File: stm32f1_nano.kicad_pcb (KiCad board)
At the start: 2 copper layers, 43.2 x 17.8 mm, 45 parts, among them J1 Analog, J2 Digital, J3 TYPE-C-31-M-12, J5 DEBUG, U1 STM32F103C8T6, U2 W25Q128JVSIQ, U4 XC6206P332MR, U5 AMS1117-5.0, Y1 X322516MLB4SI

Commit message: Change version
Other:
- board text added: "easy-smart.ch STM32F1 Nano ${REVISION}"
- board text removed: "easy-smart.ch STM32F1 Nano v1.0.1"
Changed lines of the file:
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@@
   (paper "A4")
   (title_block
-    (date "sam. 04 avril 2015")
+    (title "STM32F1 Nano")
+    (date "2023-09-05")
+    (rev "1.1.x-dev")
+    (company "easy-smart solution GmbH")
   )
   (layers
@@
     (effects (font (size 1 1) (thickness 0.15)) (justify left mirror))
   )
-  (gr_text "easy-smart.ch\nSTM32F1 Nano\nv1.0.1" (at 100.762 91.11 90) (layer "B.SilkS")
+  (gr_text "easy-smart.ch\nSTM32F1 Nano\n${REVISION}" (at 100.762 91.11 90) (layer "B.SilkS")
     (effects (font (size 0.8 0.6) (thickness 0.08)) (justify top mirror))
   )

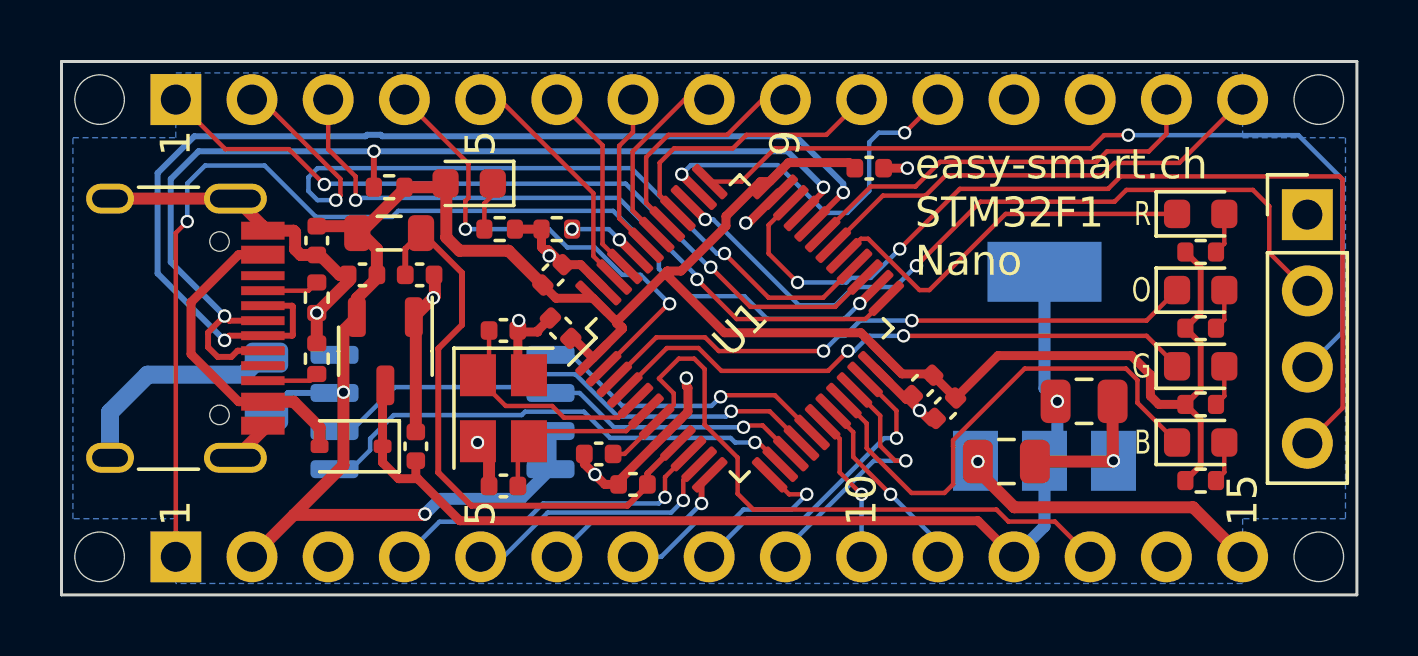
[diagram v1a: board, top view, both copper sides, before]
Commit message: #1 Make debug pins compatible with BluePill
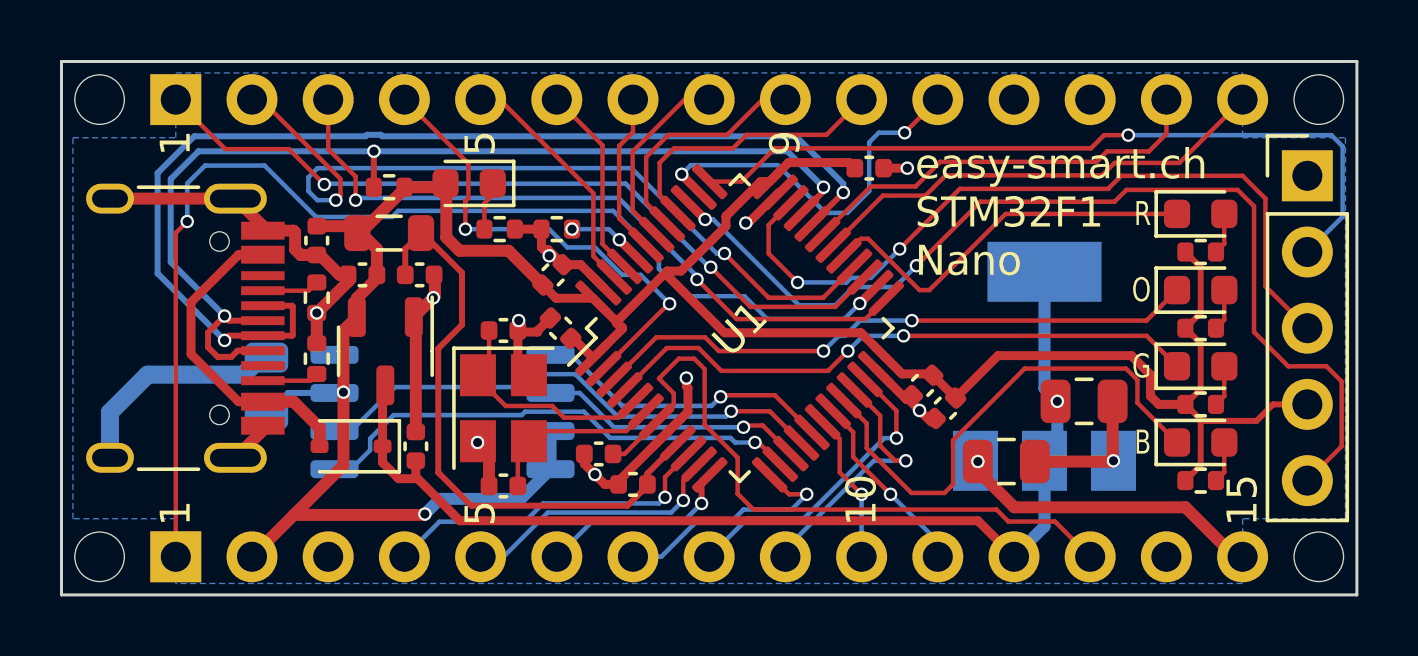
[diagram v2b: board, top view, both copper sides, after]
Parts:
- C12: value 100n 100V -> 100nF
- J5: footprint Connector_PinHeader_2.54mm:PinHeader_1x04_P2.54mm_Vertical -> Connector_PinHeader_2.54mm:PinHeader_1x05_P2.54mm_Vertical
- moved J5 1.30 mm to (141.5, 86.0)
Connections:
- J5 pad 2: SWO -> SWCLK
- J5 pad 3: SWCLK -> SWDIO
- J5 pad 4: SWDIO -> +3.3V
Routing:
- net SWO: track 25.2 -> 32.9 mm
- net SWDIO: track 32.3 -> 25.6 mm
- net +3.3V: track 82.5 -> 86.3 mm
- net SWCLK: track 29.1 -> 25.9 mm

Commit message: #5 Check PWM pins
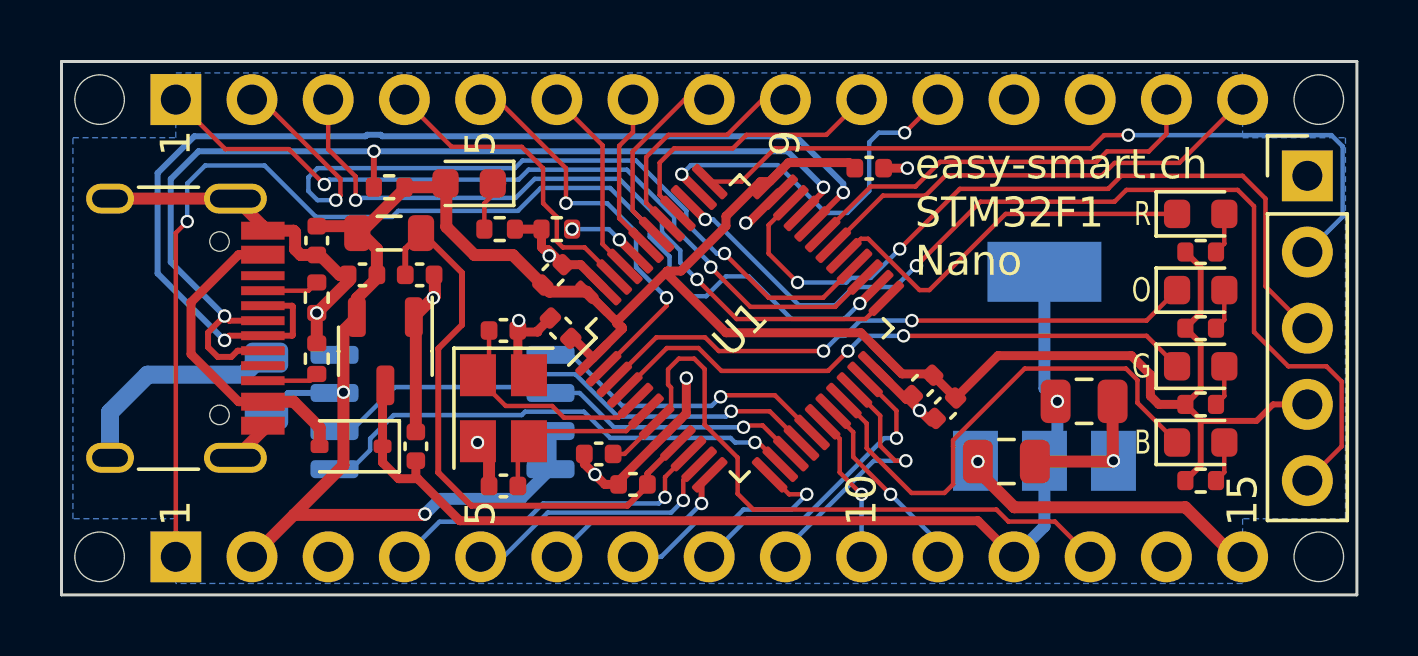
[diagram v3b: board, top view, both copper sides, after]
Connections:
- J2 pad 4: /PC13 -> /PB9
- J2 pad 5: /PB9 -> /PC13
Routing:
- net /PB9: track 7.50 -> 10.6 mm
- net /PC13: track 16.2 -> 13.5 mm
- net /PB13: track 38.0 -> 39.5 mm
- net /PB12: track 23.5 -> 24.4 mm
- net /PB14: track 26.3 -> 26.9 mm

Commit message: #4 Can U5 be moved to Front?
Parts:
- U5: moved to F.Cu
- moved C1 15.1 mm to (115.0, 89.3), turned to 45 degrees
- moved C16 4.07 mm to (130.6, 95.6), turned to 180 degrees
- moved C15 2.53 mm to (134.0, 95.6), turned to 180 degrees
- moved U5 2.29 mm to (132.3, 90.1)
- moved C2 1.34 mm to (128.2, 94.3), turned to -90 degrees
- moved C6 0.05 mm to (119.0, 96.3)
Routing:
- net /~{RESET}: track 22.6 -> 32.3 mm
- net +3.3V: track 86.0 -> 88.8 mm
- net +5V: track 35.7 -> 38.3 mm, vias 1 -> 2
- net /LED4_BLU: track 16.9 -> 19.2 mm
- net +12V: track 10.3 -> 8.16 mm, vias 1 -> 0
- net GND: track 49.7 -> 48.3 mm, vias 11 -> 12
- net SWDIO: track 25.6 -> 26.6 mm
- net SWO: track 32.9 -> 33.7 mm
- net /PB1: track 5.75 -> 6.47 mm
- net /PB11: track 10.3 -> 10.8 mm
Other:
- board text removed: "1"
- board text removed: "15"
- board text removed: "B"
- board text removed: "G"
- board text removed: "O"
- board text removed: "R"

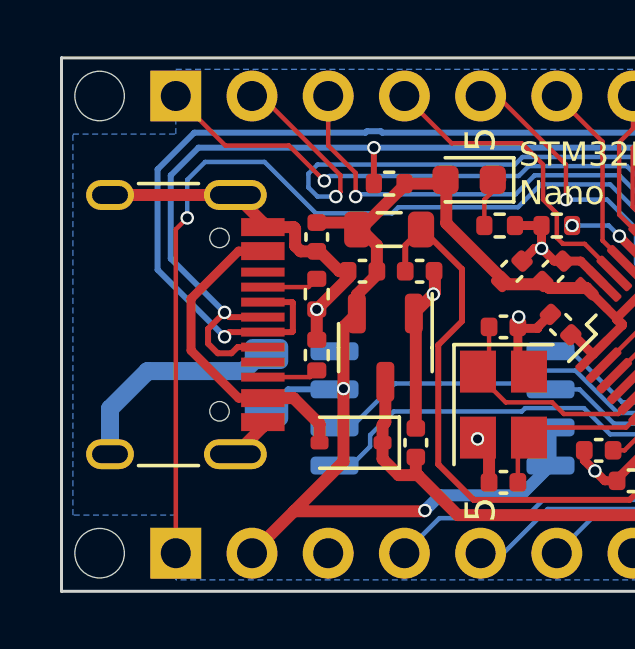
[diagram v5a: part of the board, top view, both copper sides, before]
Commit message: #10 Change USB connector to SHOU HAN TYPE-C 16PIN 2MD(073) (C2765186)
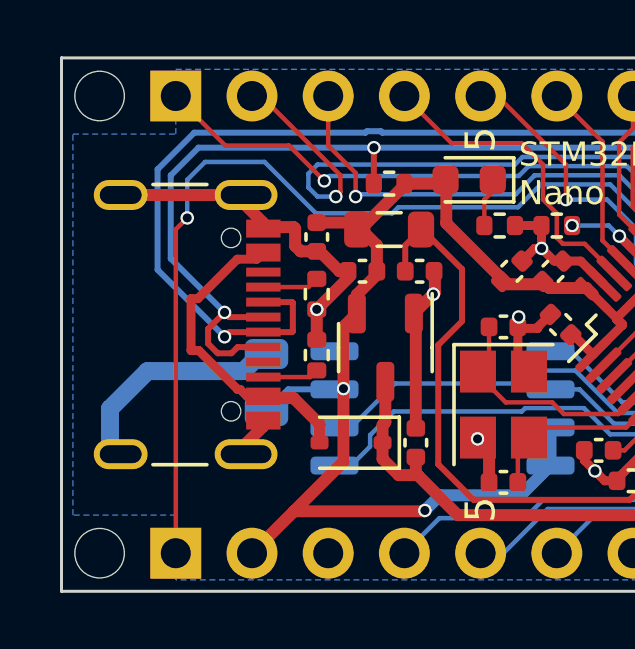
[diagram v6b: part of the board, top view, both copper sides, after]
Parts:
- C12: value 100nF -> 100n 100V
- J3: footprint Connector_USB:USB_C_Receptacle_HRO_TYPE-C-31-M-12 -> #Connector:SHOU HAN TYPE-C 16PIN 2MD(073)
- moved J3 0.38 mm to (103.0, 91.1)

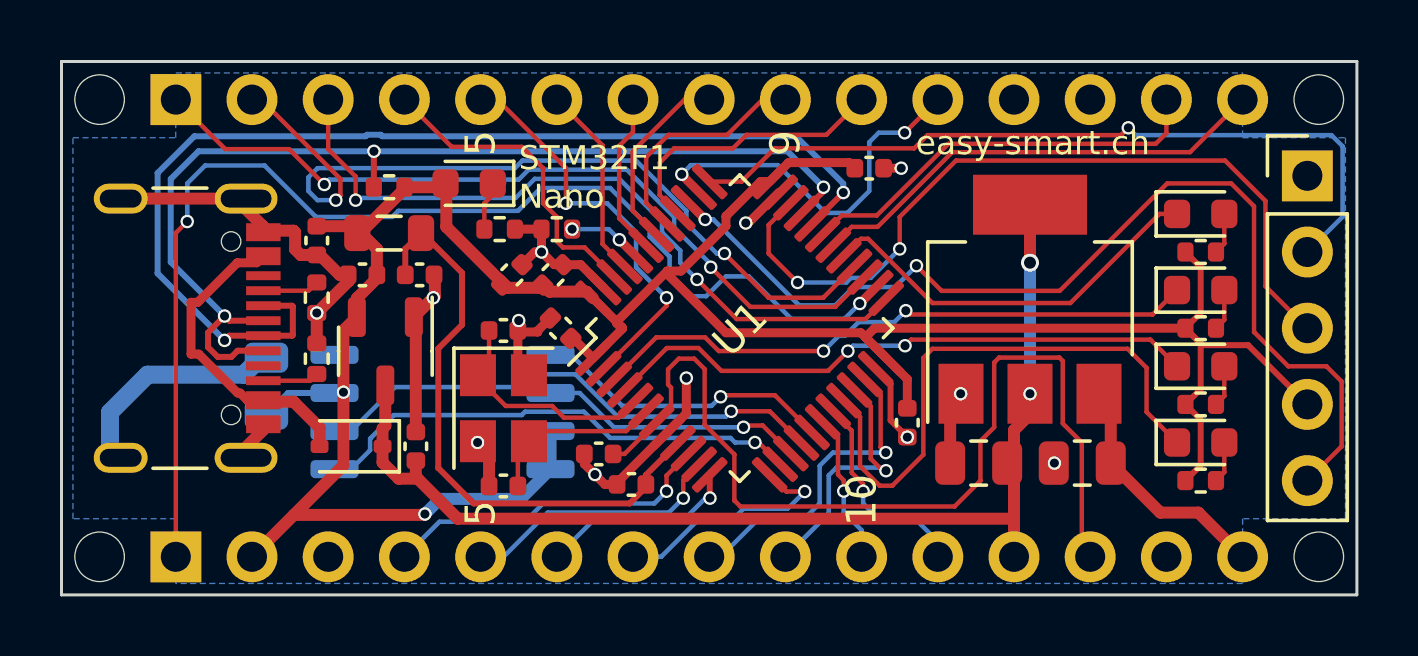
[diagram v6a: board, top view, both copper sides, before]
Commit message: #8 Use green power led
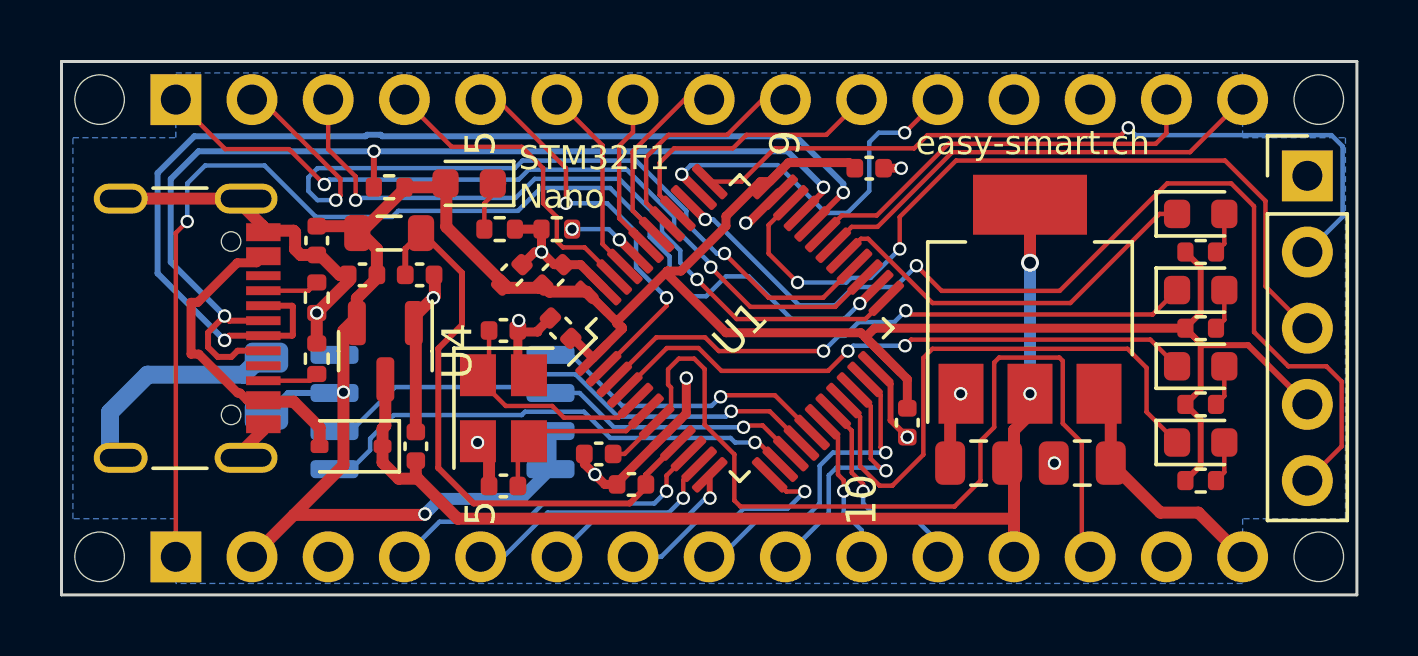
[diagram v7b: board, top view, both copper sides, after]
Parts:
- D8: value LED red (PWR) -> PWR LED (grn)
- R1: value 330 -> 200
- U4: footprint Package_TO_SOT_SMD:SOT-23-3 -> Package_TO_SOT_SMD:SOT-23
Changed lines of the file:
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@@
     (descr "Resistor SMD 0402 (1005 Metric), square (rectangular) end terminal, IPC_7351 nominal, (Body size source: IPC-SM-782 page 72, https://www.pcb-3d.com/wordpress/wp-content/uploads/ipc-sm-782a_amendment_1_and_2.pdf), generated with kicad-footprint-generator")
     (tags "resistor")
-    (property "Description" "62.5mW Thick Film Resistors ±100ppm/℃ ±1% 330Ω 0402  Chip Resistor - Surface Mount ROHS")
-    (property "JLCPCB Part #" "C25104")
+    (property "Description" "62.5mW Thick Film Resistors ±100ppm/℃ ±1% 200Ω 0402  Chip Resistor - Surface Mount ROHS")
+    (property "JLCPCB Part #" "C25087")
     (property "Manufacturer" "UNI-ROYAL(Uniroyal Elec)")
-    (property "Partnumber" "0402WGF3300TCE")
+    (property "Partnumber" "0402WGF2000TCE")
     (property "Sheetfile" "stm32f1_nano.kicad_sch")
     (property "Sheetname" "")
@@
         (effects (font (size 1 1) (thickness 0.15)))
     )
-    (fp_text value "330" (at 0 1.17) (layer "F.Fab")
+    (fp_text value "200" (at 0 1.17) (layer "F.Fab")
         (effects (font (size 1 1) (thickness 0.15)))
     )
@@
     )
   )
-  (footprint "Package_TO_SOT_SMD:SOT-23-3" (layer "F.Cu")
+  (footprint "Package_TO_SOT_SMD:SOT-23" (layer "F.Cu")
     (at 110.795 91.8775 -90)
-    (descr "SOT, 3 Pin (https://www.jedec.org/sites/default/files/docs/Mo-178D.PDF inferred 3-pin variant), generated with kicad-footprint-generator ipc_gullwing_generator.py")
+    (descr "SOT, 3 Pin (https://www.jedec.org/system/files/docs/to-236h.pdf variant AB), generated with kicad-footprint-generator ipc_gullwing_generator.py")
     (tags "SOT TO_SOT_SMD")
     (property "Description" "200mA Fixed 3.3V~3.3V Positive 6V SOT-23-3L  Linear Voltage Regulators (LDO) ROHS")
@@
     (property "ki_keywords" "Torex LDO Voltage Regulator Fixed Positive")
     (attr smd)
-    (fp_text reference "U4" (at 0 -2.4 90) (layer "F.SilkS") hide
-        (effects (font (size 1 1) (thickness 0.15)))
-    )
-    (fp_text value "XC6206P332MR" (at 0 2.4 90) (layer "F.Fab")
-        (effects (font (size 1 1) (thickness 0.15)))
-    )
-    (fp_text user "${REFERENCE}" (at 0 0 90) (layer "F.Fab")
-        (effects (font (size 0.4 0.4) (thickness 0.06)))
-    )
-    (fp_line (start 0 -1.56) (end -1.8 -1.56)
-      (stroke (width 0.12) (type solid)) (layer "F.SilkS"))
-    (fp_line (start 0 -1.56) (end 0.8 -1.56)
-      (stroke (width 0.12) (type solid)) (layer "F.SilkS"))
-    (fp_line (start 0 1.56) (end -0.8 1.56)
-      (stroke (width 0.12) (type solid)) (layer "F.SilkS"))
-    (fp_line (start 0 1.56) (end 0.8 1.56)
-      (stroke (width 0.12) (type solid)) (layer "F.SilkS"))
-    (fp_line (start -2.05 -1.7) (end -2.05 1.7)
-      (stroke (width 0.05) (type solid)) (layer "F.CrtYd"))
-    (fp_line (start -2.05 1.7) (end 2.05 1.7)
-      (stroke (width 0.05) (type solid)) (layer "F.CrtYd"))
-    (fp_line (start 2.05 -1.7) (end -2.05 -1.7)
-      (stroke (width 0.05) (type solid)) (layer "F.CrtYd"))
-    (fp_line (start 2.05 1.7) (end 2.05 -1.7)
-      (stroke (width 0.05) (type solid)) (layer "F.CrtYd"))
-    (fp_line (start -0.8 -1.05) (end -0.4 -1.45)
-      (stroke (width 0.1) (type solid)) (layer "F.Fab"))
-    (fp_line (start -0.8 1.45) (end -0.8 -1.05)
-      (stroke (width 0.1) (type solid)) (layer "F.Fab"))
-    (fp_line (start -0.4 -1.45) (end 0.8 -1.45)
-      (stroke (width 0.1) (type solid)) (layer "F.Fab"))
-    (fp_line (start 0.8 -1.45) (end 0.8 1.45)
-      (stroke (width 0.1) (type solid)) (layer "F.Fab"))
-    (fp_line (start 0.8 1.45) (end -0.8 1.45)
-      (stroke (width 0.1) (type solid)) (layer "F.Fab"))
-    (pad "1" smd roundrect (at -1.1375 -0.95 270) (size 1.325 0.6) (layers "F.Cu" "F.Paste" "F.Mask") (roundrect_rratio 0.25)
+    (fp_text reference "U4" (at 0 -2.4 -90) (layer "F.SilkS")
+        (effects (font (size 1 1) (thickness 0.15)))
+    )
+    (fp_text value "XC6206P332MR" (at 0 2.4 -90) (layer "F.Fab")
+        (effects (font (size 1 1) (thickness 0.15)))
+    )
+    (fp_text user "${REFERENCE}" (at 0 0 -90) (layer "F.Fab")
+        (effects (font (size 0.32 0.32) (thickness 0.05)))
+    )
+    (fp_line (start 0 -1.56) (end -1.675 -1.56)
+      (stroke (width 0.12) (type solid)) (layer "F.SilkS"))
+    (fp_line (start 0 -1.56) (end 0.65 -1.56)
+      (stroke (width 0.12) (type solid)) (layer "F.SilkS"))
+    (fp_line (start 0 1.56) (end -0.65 1.56)
+      (stroke (width 0.12) (type solid)) (layer "F.SilkS"))
+    (fp_line (start 0 1.56) (end 0.65 1.56)
+      (stroke (width 0.12) (type solid)) (layer "F.SilkS"))
+    (fp_line (start -1.92 -1.7) (end -1.92 1.7)
+      (stroke (width 0.05) (type solid)) (layer "F.CrtYd"))
+    (fp_line (start -1.92 1.7) (end 1.92 1.7)
+      (stroke (width 0.05) (type solid)) (layer "F.CrtYd"))
+    (fp_line (start 1.92 -1.7) (end -1.92 -1.7)
+      (stroke (width 0.05) (type solid)) (layer "F.CrtYd"))
+    (fp_line (start 1.92 1.7) (end 1.92 -1.7)
+      (stroke (width 0.05) (type solid)) (layer "F.CrtYd"))
+    (fp_line (start -0.65 -1.125) (end -0.325 -1.45)
+      (stroke (width 0.1) (type solid)) (layer "F.Fab"))
+    (fp_line (start -0.65 1.45) (end -0.65 -1.125)
+      (stroke (width 0.1) (type solid)) (layer "F.Fab"))
+    (fp_line (start -0.325 -1.45) (end 0.65 -1.45)
+      (stroke (width 0.1) (type solid)) (layer "F.Fab"))
+    (fp_line (start 0.65 -1.45) (end 0.65 1.45)
+      (stroke (width 0.1) (type solid)) (layer "F.Fab"))
+    (fp_line (start 0.65 1.45) (end -0.65 1.45)
+      (stroke (width 0.1) (type solid)) (layer "F.Fab"))
+    (pad "1" smd roundrect (at -0.9375 -0.95 270) (size 1.475 0.6) (layers "F.Cu" "F.Paste" "F.Mask") (roundrect_rratio 0.25)
       (net 1 "GND") (pinfunction "GND") (pintype "power_in"))
-    (pad "2" smd roundrect (at -1.1375 0.95 270) (size 1.325 0.6) (layers "F.Cu" "F.Paste" "F.Mask") (roundrect_rratio 0.25)
+    (pad "2" smd roundrect (at -0.9375 0.95 270) (size 1.475 0.6) (layers "F.Cu" "F.Paste" "F.Mask") (roundrect_rratio 0.25)
       (net 3 "+3.3V") (pinfunction "VO") (pintype "power_out"))
-    (pad "3" smd roundrect (at 1.1375 0 270) (size 1.325 0.6) (layers "F.Cu" "F.Paste" "F.Mask") (roundrect_rratio 0.25)
+    (pad "3" smd roundrect (at 0.9375 0 270) (size 1.475 0.6) (layers "F.Cu" "F.Paste" "F.Mask") (roundrect_rratio 0.25)
       (net 9 "+5V") (pinfunction "VI") (pintype "power_in"))
-    (model "${KICAD6_3DMODEL_DIR}/Package_TO_SOT_SMD.3dshapes/SOT-23-3.wrl"
+    (model "${KICAD6_3DMODEL_DIR}/Package_TO_SOT_SMD.3dshapes/SOT-23.wrl"
       (offset (xyz 0 0 0))
       (scale (xyz 1 1 1))
@@
     (descr "LED SMD 0603 (1608 Metric), square (rectangular) end terminal, IPC_7351 nominal, (Body size source: http://www.tortai-tech.com/upload/download/2011102023233369053.pdf), generated with kicad-footprint-generator")
     (tags "LED")
-    (property "Description" "-40℃~+85℃ Red 0603  Light Emitting Diodes (LED) ROHS")
-    (property "JLCPCB Part #" "C2286")
-    (property "Manufacturer" "Hubei KENTO Elec")
-    (property "Manufacturer_Name" "Hubei KENTO Elec")
-    (property "Manufacturer_Part_Number" "KT-0603R")
-    (property "Partnumber" "KT-0603R")
+    (property "Description" "Colorless transparence -40℃~+85℃ 520nm~535nm Emerald 120° 110mW 0603  Light Emitting Diodes (LED) ROHS")
+    (property "JLCPCB Part #" "C72043")
+    (property "Manufacturer" "Everlight Elec")
+    (property "Manufacturer_Name" "Everlight Elec")
+    (property "Manufacturer_Part_Number" "19-217/GHC-YR1S2/3T")
+    (property "Partnumber" "19-217/GHC-YR1S2/3T")
     (property "Sheetfile" "stm32f1_nano.kicad_sch")
     (property "Sheetname" "")
@@
         (effects (font (size 1 1) (thickness 0.15)))
     )
-    (fp_text value "LED red (PWR)" (at 0 1.43) (layer "F.Fab")
-        (effects (font (size 1 1) (thickness 0.15)))
-    )
+    (fp_text value "PWR LED (grn)" (at 0 1.43) (layer "F.Fab")
+        (effects (font (size 1 1) (thickness 0.15)))
+    )
